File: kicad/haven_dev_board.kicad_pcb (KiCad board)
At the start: 6 copper layers, 72.9 x 160.9 mm, 89 parts, among them CN1 BM46B-12DS-0.35V(51).1, J1 CLE-107-01-G-DV.1, Q1 CSD23382F4.1, Q2 CSD13380F3T.1, Q3 CSD13380F3T.1, SW1 TS2819A 230GF.1, U1 BMX160.1, U10 SN74AXC4T774RSVR.1, U12 GT-USB-9047A.1, U13 SPH0641LU4H-1.1, U14 MX25R6435FBFIL0.1, U15 ADAU1860BCBZRL.1, U2 BQ25120AYFPR.1, U3 AP22916BCA4-7.1, U4 XL-0201SURC.1, U5 KTD2026.1, U6 BQ27220YZFR.1, U8 1MΩ.1, U9 AP22916BCA4-7.1, X1 Q13FC1350000200.1

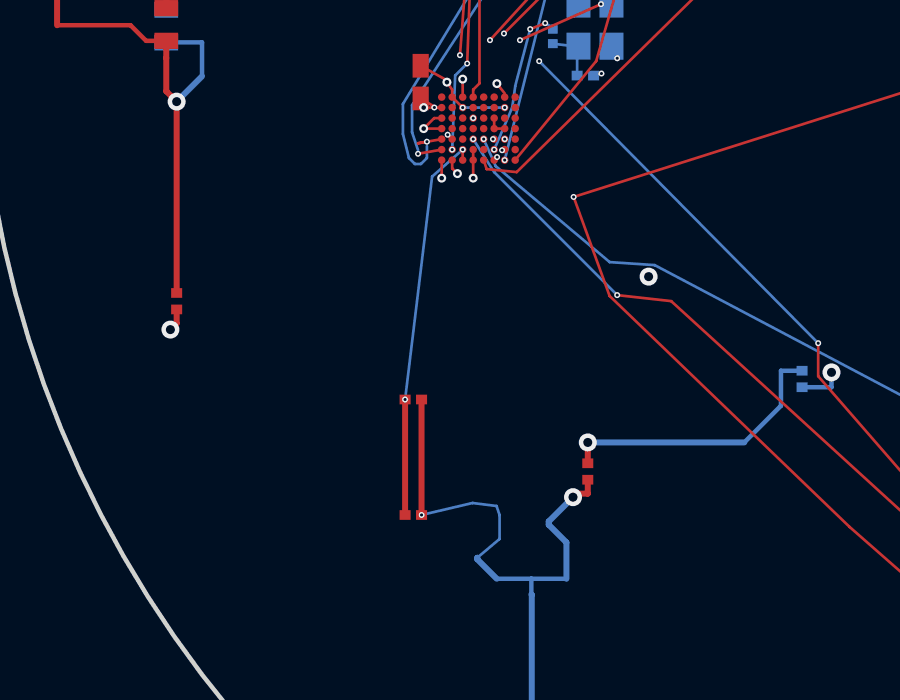
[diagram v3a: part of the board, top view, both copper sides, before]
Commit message: Move C31 (100 nF on U15's $1N151 node) to 1.3 mm from balls A3/B3; DRC 219 -> 219, 0 new
C31 was catalogued as U14's decoupling in the placement review; the netlist
says otherwise -- its non-GND pad is $1N151, the ADAU1860's A3/B3 node, so
it is a codec bypass cap that sat 13 mm away at (56.45,124.33). Now at
(58.89,113.32) on F.Cu directly below the BGA. The 3.8 mm F.Cu feed plus
B.Cu stub that used to reach the old position removed as dangling.

Tool fixes from this stage: hole-to-hole checks now use each existing
via's real drill (the board mixes 0.10 and 0.15 mm drills; assuming 0.10
produced a 0.1806 mm miss), a route's own vias are checked against each
other, and the multilayer via penalty is raised so decoupling routes stay
single-layer where possible. tools/stage.sh: one DRC-gated stage per run,
restores the board unless zero new violation identities.

kicad-cli 9.0.8: 219 violations / 2 unconnected before and after.

Co-Authored-By: Claude Fable 5.1 <noreply@anthropic.com>
Claude-Session: https://claude.ai/code/session_01K7G9Bv5agmyedmt776NSLV
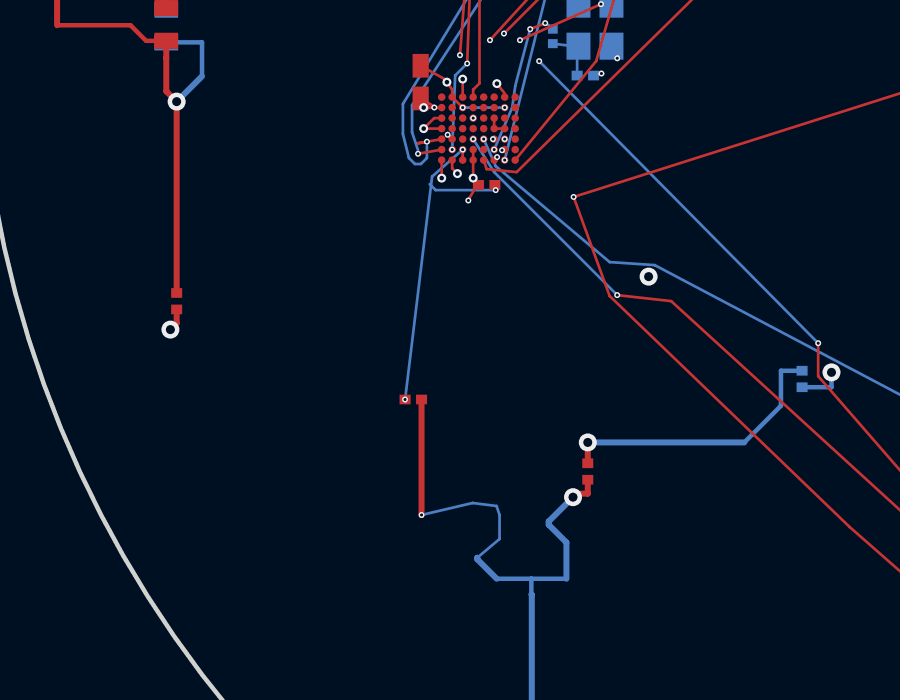
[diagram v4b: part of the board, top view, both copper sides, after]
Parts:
- moved C31 11.3 mm to (58.9, 113.3), turned to 180 degrees
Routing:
- net $1N151: track 13.0 -> 11.7 mm, vias 2 -> 3
- net GND: track 662.1 -> 662.7 mm, vias 63 -> 64
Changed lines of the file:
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@@
 	(footprint "haven_footprints:C0201"
 		(layer "F.Cu")
-		(at 56.4453 124.3272)
+		(at 58.89 113.323 180)
 		(property "Reference" "C31"
-			(at 0 -1.5 0)
+			(at 0 -1.5 180)
 			(layer "F.SilkS")
 			(hide yes)
@@
 		)
 		(property "Value" "100nF.1"
-			(at 0 1.5 0)
+			(at 0 1.5 180)
 			(layer "F.Fab")
 			(hide yes)
@@
 		)
 		(property "Datasheet" ""
-			(at 0 0 0)
+			(at 0 0 180)
 			(layer "F.Fab")
 			(hide yes)
@@
 		)
 		(property "Description" ""
-			(at 0 0 0)
+			(at 0 0 180)
 			(layer "F.Fab")
 			(hide yes)
@@
 		(attr smd)
 		(pad "1" smd rect
-			(at -0.2743 0)
+			(at -0.2743 0 180)
 			(size 0.3684 0.324)
 			(layers "F.Cu" "F.Mask" "F.Paste")
@@
 		)
 		(pad "2" smd rect
-			(at 0.2741 0)
+			(at 0.2741 0 180)
 			(size 0.3684 0.324)
 			(layers "F.Cu" "F.Mask" "F.Paste")
@@
 	)
 	(segment
-		(start 56.171 120.4777)
-		(end 56.171 124.3272)
-		(width 0.2)
-		(locked yes)
-		(layer "F.Cu")
-		(net 4)
-	)
-	(segment
 		(start 58.0904 112.4979)
 		(end 58.0904 112.1479)
@@
 	)
 	(segment
-		(start 56.171 124.327)
-		(end 56.171 124.3272)
-		(width 0.2)
+		(start 59.1904 113.4979)
+		(end 59.1904 113.2979)
+		(width 0.09)
 		(layer "F.Cu")
 		(net 4)
@@
 	)
 	(via
+		(at 59.1904 113.4979)
+		(size 0.2)
+		(drill 0.1)
+		(layers "F.Cu" "B.Cu")
+		(net 4)
+	)
+	(via
 		(at 58.0904 112.1479)
 		(size 0.2)
@@
 	)
 	(segment
+		(start 56.9904 113.2979)
+		(end 57.1904 113.4979)
+		(width 0.09)
+		(layer "B.Cu")
+		(net 4)
+	)
+	(segment
+		(start 57.1904 113.4979)
+		(end 59.1904 113.4979)
+		(width 0.09)
+		(layer "B.Cu")
+		(net 4)
+	)
+	(segment
 		(start 58.0904 112.1479)
 		(end 57.071 113.0479)
@@
 	)
 	(segment
+		(start 58.578094 113.323)
+		(end 58.278094 113.823)
+		(width 0.09)
+		(layer "F.Cu")
+		(net 25)
+	)
+	(segment
 		(start 83.6341 95.3277)
 		(end 84.12 95.3277)
@@
 		(net 25)
 	)
+	(via
+		(at 58.278094 113.843442)
+		(size 0.2)
+		(drill 0.1)
+		(layers "F.Cu" "B.Cu")
+		(net 25)
+	)

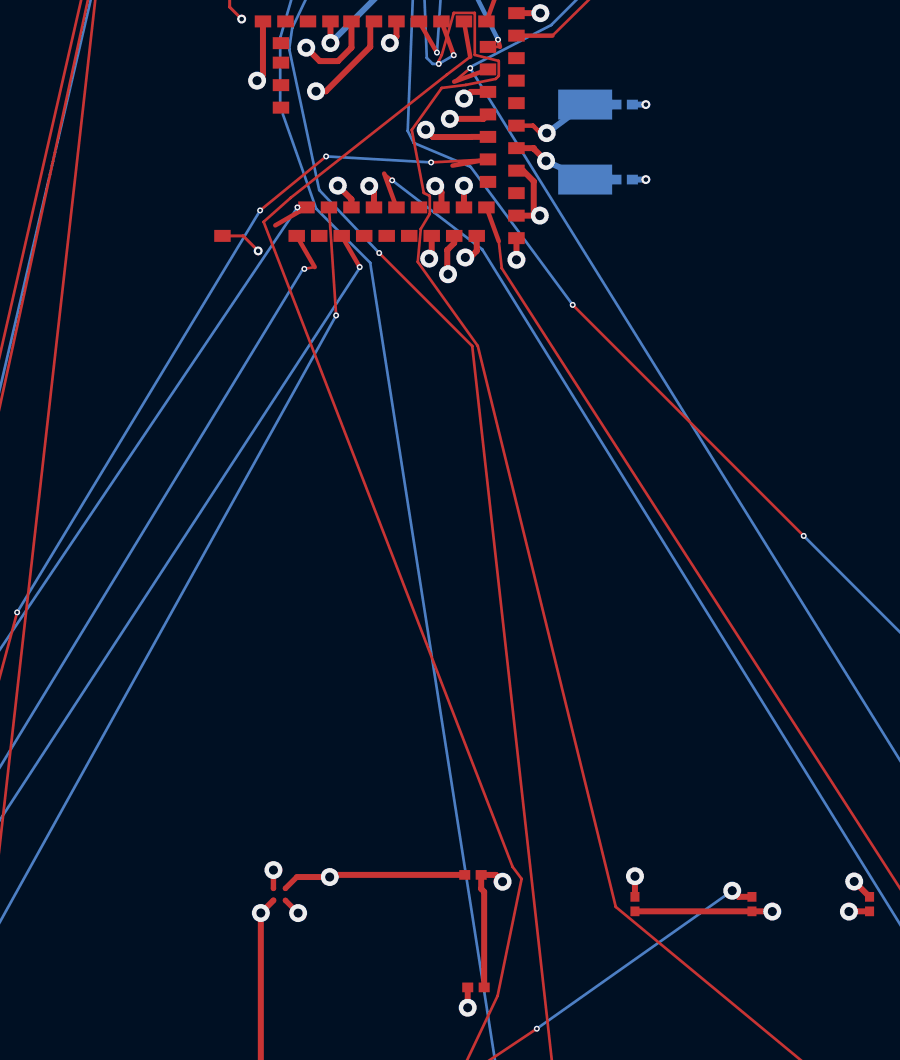
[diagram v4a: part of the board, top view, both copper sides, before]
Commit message: Move C1 (+1.8V 1 uF) to 1.0 mm from MDBT531 pins 38/41; DRC 219 -> 219, 0 new
The +1.8V rail's only nearby cap was 25.9 mm from the module (and 29.5 mm
from U15, which turns out to have no +1.8V ball at all -- its supply is
V_LS, handled by C33). Now on F.Cu just east of the module edge, rail pad
routed to pin 38, GND pad on its own via. Dangling remnant of the old feed
removed. B.Cu under the module was tried first and is unusable for vias
(module pads), so this stage was run with --layer F.Cu.

kicad-cli 9.0.8: 219 violations / 2 unconnected before and after.

Co-Authored-By: Claude Fable 5.1 <noreply@anthropic.com>
Claude-Session: https://claude.ai/code/session_01K7G9Bv5agmyedmt776NSLV
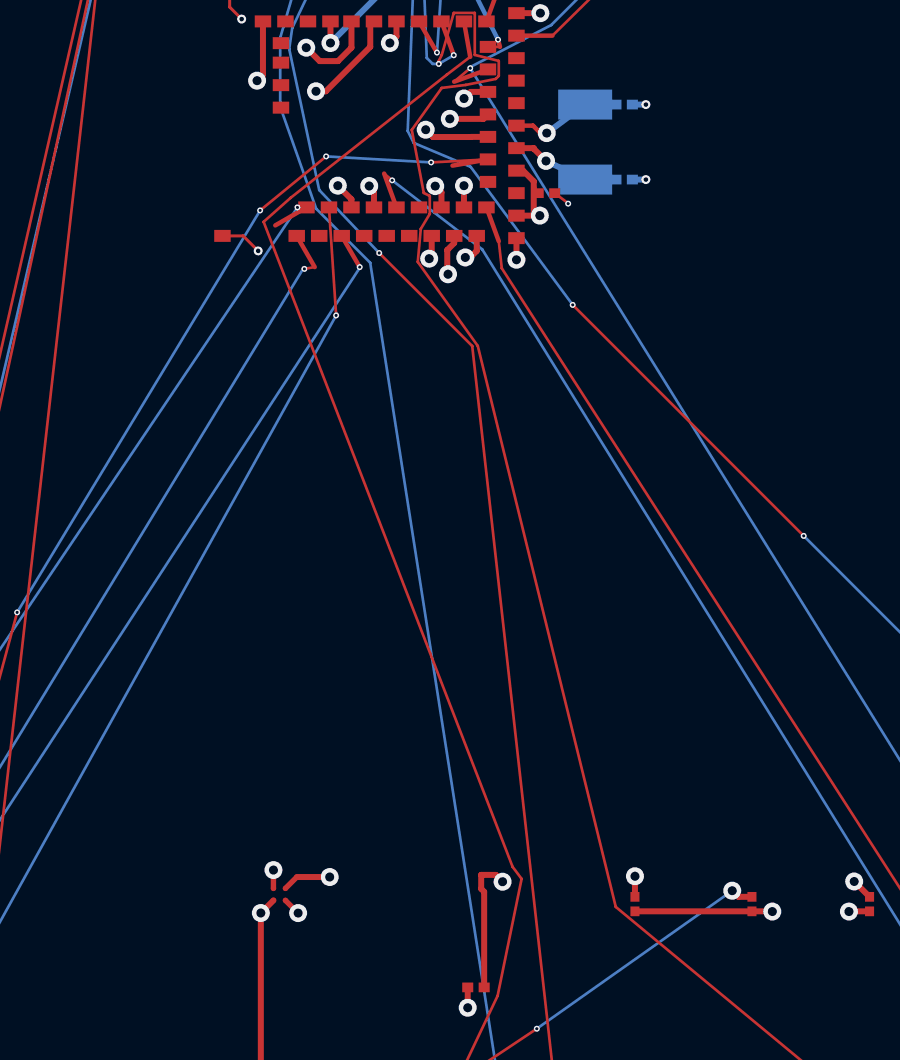
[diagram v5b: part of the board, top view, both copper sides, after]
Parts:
- moved C1 22.9 mm to (85.8, 72.6)
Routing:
- net +1.8V: track 181.5 -> 177.5 mm
- net GND: track 662.7 -> 663.2 mm, vias 64 -> 65
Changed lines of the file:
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@@
 	(footprint "haven_footprints:C0201"
 		(layer "F.Cu")
-		(at 83.3598 95.3277)
+		(at 85.81 72.603)
 		(property "Reference" "C1"
 			(at 0 -1.5 0)
@@
 	)
 	(segment
-		(start 83.0857 95.3277)
-		(end 78.6556 95.3277)
-		(width 0.2)
-		(locked yes)
-		(layer "F.Cu")
-		(net 14)
-	)
-	(segment
 		(start 106.3669 42.8025)
 		(end 106.6128 43.0484)
@@
 	)
 	(segment
+		(start 85.3869 72.2094)
+		(end 85.486899 72.6094)
+		(width 0.09)
+		(layer "F.Cu")
+		(net 14)
+	)
+	(segment
 		(start 106.6128 43.0484)
 		(end 106.6128 43.0836)
@@
 	)
 	(segment
+		(start 86.0843 72.603)
+		(end 86.4843 72.902999)
+		(width 0.09)
+		(layer "F.Cu")
+		(net 25)
+	)
+	(segment
 		(start 47.0765 106.0201)
 		(end 47.37 106.0201)
@@
 		(net 25)
 	)
+	(via
+		(at 86.534 72.952999)
+		(size 0.2)
+		(drill 0.1)
+		(layers "F.Cu" "B.Cu")
+		(net 25)
+	)

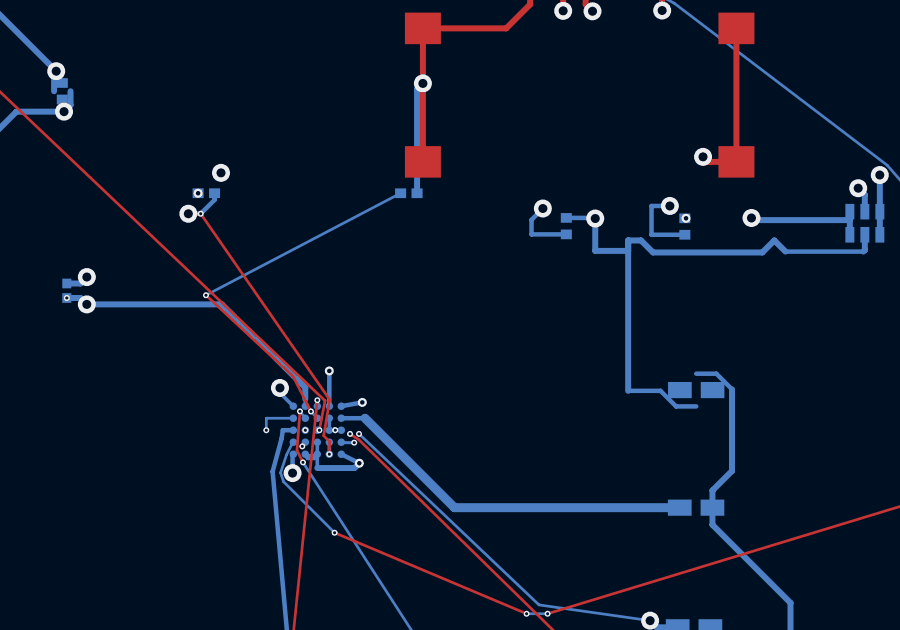
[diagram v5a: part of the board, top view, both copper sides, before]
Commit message: Move C22 (VUSB) to 1.0 mm from U2; DRC 219 -> 219, 0 new
C22 was 10.7 mm from the charger's VUSB ball A2; now beside U2 on F.Cu with
VUSB reached by stitching a new 0.20/0.10 via onto the rail's In1.Cu run
just outside the DSBGA escape field (the ball itself and its escape via are
hemmed in at 0.4 mm pitch), GND on its own via. Dangling remnants of the old
feed removed.

Tool fixes this stage (all caught by the DRC gate, none by inspection):
- placement_lib.find_spot evaluated candidates un-flipped; move() flips the
  part when the layer changes, mirroring the pads, so a check could clear a
  spot whose real pad lands 0.193 mm from a via. It now flips for the test.
- anchors carry their layer (a U2 ball is B.Cu copper; routing F.Cu copper
  from it connects nothing); inner-layer track ends are never anchors;
  inner-layer runs of the net can be via-stitched away from the IC.
- routes use the .kicad_dru per-pair clearance exceptions of the net being
  routed (never looser than the rules), at 0.215 mm otherwise to absorb
  grid/simplification rounding.
- GND routes constrain the pad end (part layer), not the via end.

kicad-cli 9.0.8: 219 violations / 2 unconnected before and after.

Co-Authored-By: Claude Fable 5.1 <noreply@anthropic.com>
Claude-Session: https://claude.ai/code/session_01K7G9Bv5agmyedmt776NSLV
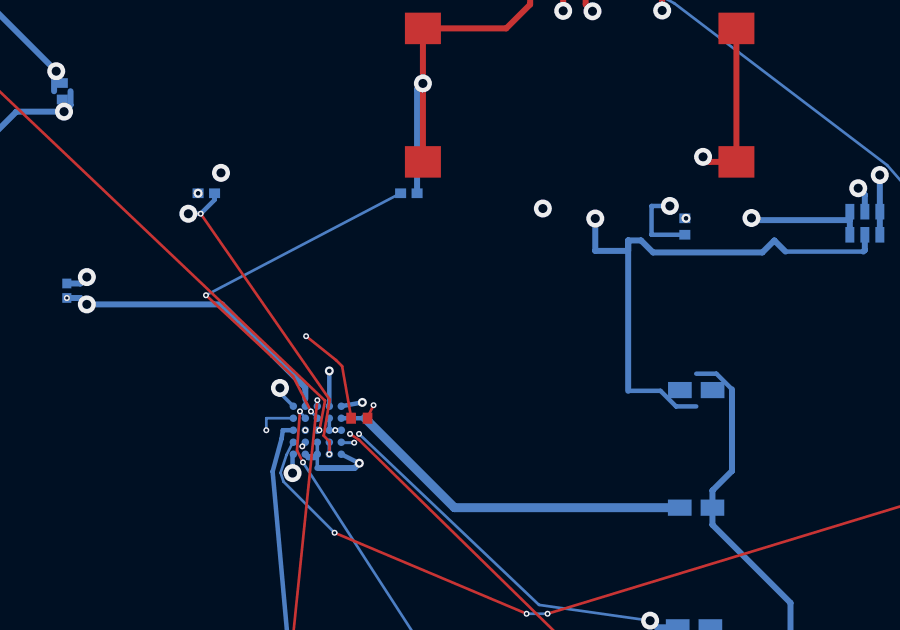
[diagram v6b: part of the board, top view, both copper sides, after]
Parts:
- C22: moved to F.Cu
- moved C22 9.41 mm to (67.9, 32.5), turned to 90 degrees
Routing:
- net VUSB: track 169.6 -> 170.7 mm, vias 6 -> 7
- net GND: track 663.2 -> 662.7 mm, vias 65 -> 66
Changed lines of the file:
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@@
 		(embedded_fonts no)
 	)
+	(footprint "haven_footprints:C0201"
+		(layer "F.Cu")
+		(at 67.91 32.476999 90)
+		(property "Reference" "C22"
+			(at 0 1.5 270)
+			(layer "F.SilkS")
+			(hide yes)
+			(effects
+				(font
+					(size 0.8 0.8)
+					(thickness 0.12)
+				)
+				(justify mirror)
+			)
+		)
+		(property "Value" "1uF >10V.1"
+			(at 0 -1.5 270)
+			(layer "F.Fab")
+			(hide yes)
+			(effects
+				(font
+					(size 0.8 0.8)
+					(thickness 0.12)
+				)
+				(justify mirror)
+			)
+		)
+		(property "Datasheet" ""
+			(at 0 0 270)
+			(layer "B.Fab")
+			(hide yes)
+			(effects
+				(font
+					(size 1.27 1.27)
+					(thickness 0.15)
+				)
+				(justify mirror)
+			)
+		)
+		(property "Description" ""
+			(at 0 0 270)
+			(layer "B.Fab")
+			(hide yes)
+			(effects
+				(font
+					(size 1.27 1.27)
+					(thickness 0.15)
+				)
+				(justify mirror)
+			)
+		)
+		(attr smd)
+		(pad "1" smd rect
+			(at 0.0001 -0.2743 90)
+			(size 0.3684 0.324)
+			(layers "F.Cu" "F.Mask" "F.Paste")
+			(net 76 "VUSB")
+		)
+		(pad "2" smd rect
+			(at 0.0001 0.2743 90)
+			(size 0.3684 0.324)
+			(layers "F.Cu" "F.Mask" "F.Paste")
+			(net 25 "GND")
+		)
+		(embedded_fonts no)
+	)
 	(footprint "haven_footprints:WLCSP-22_MX25R6435FBFIL0"
 		(layer "F.Cu")
@@
 		(embedded_fonts no)
 	)
-	(footprint "haven_footprints:C0201"
-		(layer "B.Cu")
-		(at 74.8098 26.0747)
-		(property "Reference" "C22"
-			(at 0 -1.5 0)
-			(layer "B.SilkS")
-			(hide yes)
-			(effects
-				(font
-					(size 0.8 0.8)
-					(thickness 0.12)
-				)
-			)
-		)
-		(property "Value" "1uF >10V.1"
-			(at 0 1.5 0)
-			(layer "B.Fab")
-			(hide yes)
-			(effects
-				(font
-					(size 0.8 0.8)
-					(thickness 0.12)
-				)
-			)
-		)
-		(property "Datasheet" ""
-			(at 0 0 0)
-			(layer "F.Fab")
-			(hide yes)
-			(effects
-				(font
-					(size 1.27 1.27)
-					(thickness 0.15)
-				)
-			)
-		)
-		(property "Description" ""
-			(at 0 0 0)
-			(layer "F.Fab")
-			(hide yes)
-			(effects
-				(font
-					(size 1.27 1.27)
-					(thickness 0.15)
-				)
-			)
-		)
-		(attr smd)
-		(pad "1" smd rect
-			(at 0.0001 0.2743)
-			(size 0.3684 0.324)
-			(layers "B.Cu" "B.Mask" "B.Paste")
-			(net 76 "VUSB")
-		)
-		(pad "2" smd rect
-			(at 0.0001 -0.2743)
-			(size 0.3684 0.324)
-			(layers "B.Cu" "B.Mask" "B.Paste")
-			(net 25 "GND")
-		)
-		(embedded_fonts no)
-	)
 	(footprint "haven_footprints:b5c2858cad4e462ab76a8d0ccf4ade45"
 		(layer "B.Cu")
@@
 	)
 	(segment
+		(start 68.3843 32.043987)
+		(end 68.1843 32.443987)
+		(width 0.09)
+		(layer "F.Cu")
+		(net 25)
+	)
+	(segment
 		(start 108.6309 96.902)
 		(end 108.6307 96.9018)
@@
 	)
 	(via
+		(at 68.384 32.043987)
+		(size 0.2)
+		(drill 0.1)
+		(layers "F.Cu" "B.Cu")
+		(net 25)
+	)
+	(via
 		(at 56.1147 102.3807)
 		(size 0.6)
@@
 	)
 	(segment
-		(start 74.8099 25.8004)
-		(end 75.7541 25.8004)
-		(width 0.15)
-		(locked yes)
-		(layer "B.Cu")
-		(net 25)
-	)
-	(segment
 		(start 78.4104 111.4031)
 		(end 78.4104 111.4016)
@@
 	)
 	(segment
+		(start 67.335618 30.742281)
+		(end 67.635618 32.442281)
+		(width 0.09)
+		(layer "F.Cu")
+		(net 76)
+	)
+	(segment
 		(start 104.3099 96.5443)
 		(end 103.8567 96.5443)
@@
 		(net 76)
 	)
+	(segment
+		(start 66.135618 29.742281)
+		(end 67.135618 30.542281)
+		(width 0.09)
+		(layer "F.Cu")
+		(net 76)
+	)
+	(segment
+		(start 67.135618 30.542281)
+		(end 67.335618 30.742281)
+		(width 0.09)
+		(layer "F.Cu")
+		(net 76)
+	)
 	(via
 		(at 74.0279 25.4868)
@@
 	)
 	(via
+		(at 66.135618 29.742281)
+		(size 0.2)
+		(drill 0.1)
+		(layers "F.Cu" "B.Cu")
+		(net 76)
+	)
+	(via
 		(at 76.4866 4.8447)
 		(size 0.6)
@@
 	)
 	(segment
-		(start 73.65 25.8647)
-		(end 73.65 26.349)
-		(width 0.15)
-		(locked yes)
-		(layer "B.Cu")
-		(net 76)
-	)
-	(segment
 		(start 84.5397 24.8102)
 		(end 84.7605 25.031)
@@
 	)
 	(segment
-		(start 73.65 26.349)
-		(end 74.8099 26.349)
-		(width 0.15)
-		(locked yes)
-		(layer "B.Cu")
-		(net 76)
-	)
-	(segment
 		(start 76.2598 3.5912)
 		(end 76.2598 4.6179)
@@
 		(locked yes)
 		(layer "B.Cu")
-		(net 76)
-	)
-	(segment
-		(start 74.0279 25.4868)
-		(end 73.65 25.8647)
-		(width 0.15)
-		(locked yes)
-		(layer "B.Cu")
